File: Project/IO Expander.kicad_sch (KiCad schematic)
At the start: 32 parts, among them J801 Conn_02x08_Odd_Even, U801 MCP23017T-E_ML

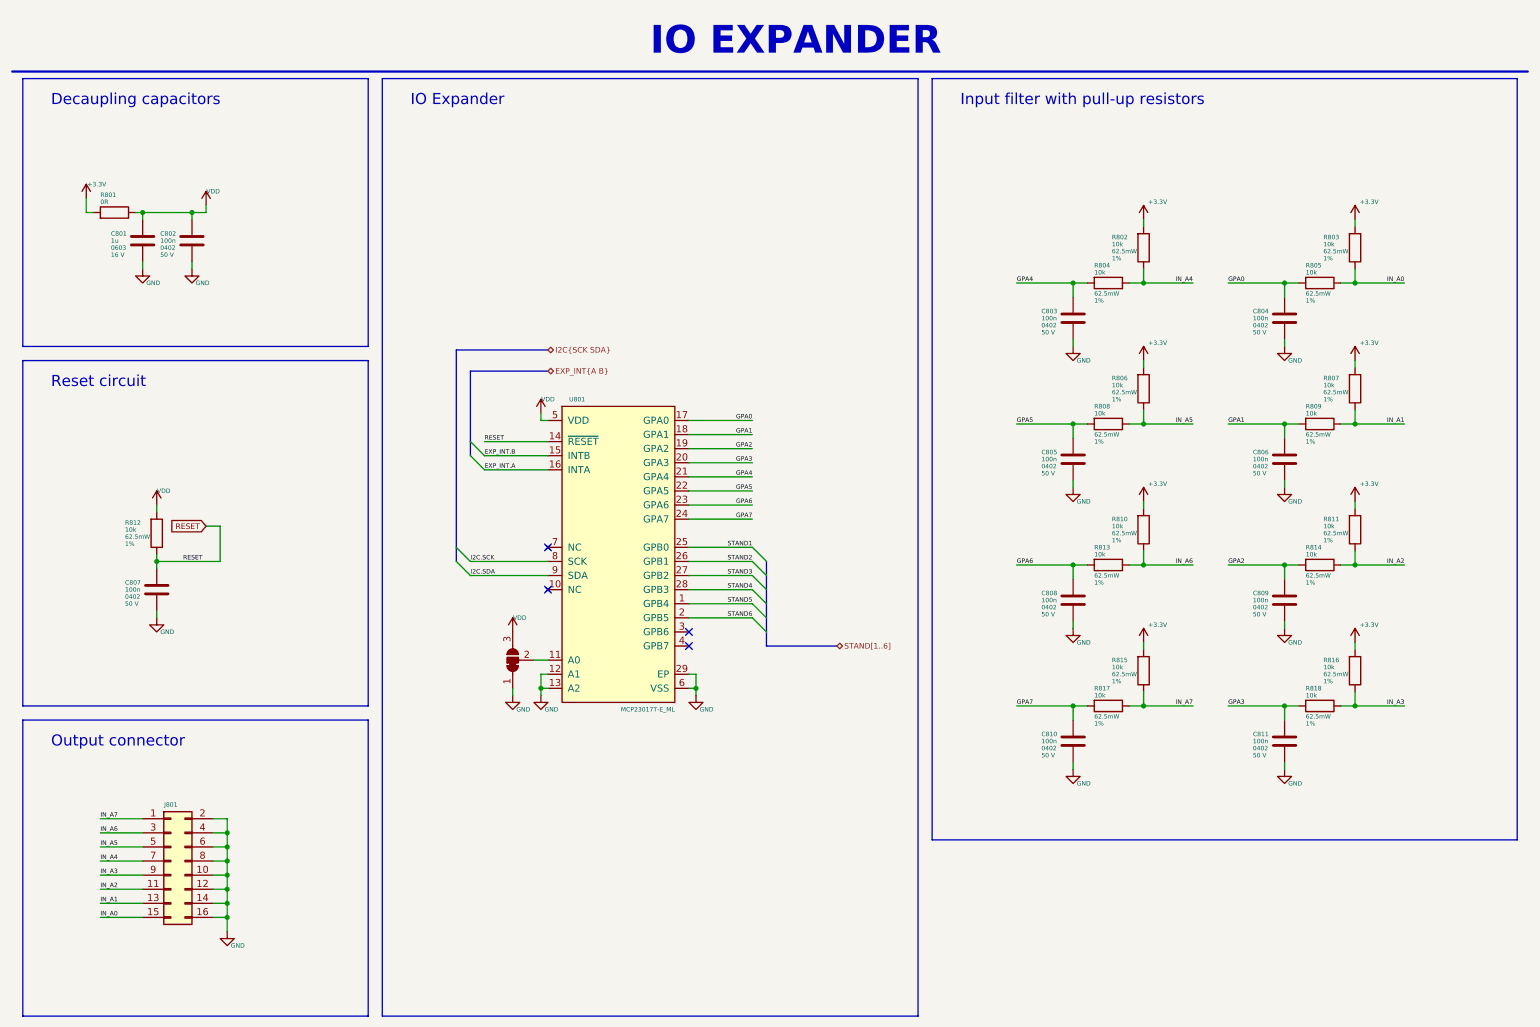
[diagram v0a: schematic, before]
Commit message: Cleaning files, added testpoints
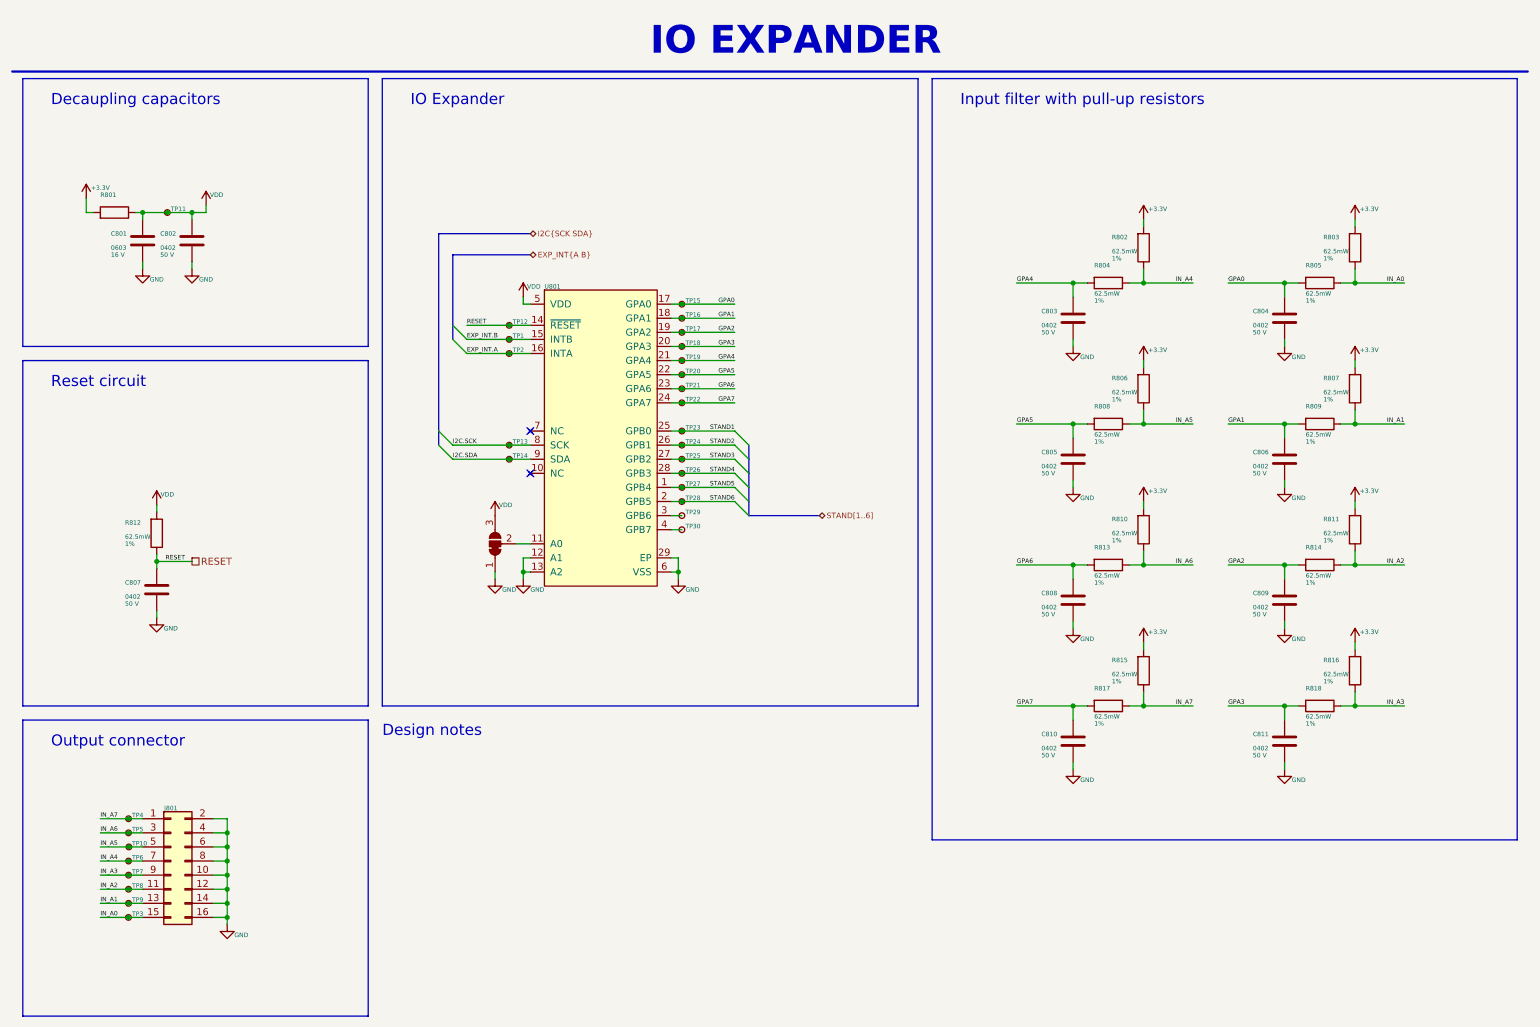
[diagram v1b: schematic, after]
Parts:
- added TP1, TP10, TP11, TP12, TP13, TP14, TP15, TP16, TP17, TP18, TP19, TP2, TP20, TP21, TP22, TP23, TP24, TP25, TP26, TP27, TP28, TP29, TP3, TP30, TP4, TP5, TP6, TP7, TP8, TP9: (no value), symbol Connector:TestPoint_Small
- C801: value 1u -> (none); footprint Capacitor_SMD:C_0603_1608Metric -> (none)
- C802, C803, C804, C805, C806, C807, C808, C809, C810, C811: value 100n -> (none); footprint Capacitor_SMD:C_0402_1005Metric -> (none)
- J801: value Conn_02x08_Odd_Even -> (none); footprint Connector_PinHeader_2.54mm:PinHeader_2x08_P2.54mm_Vertical -> (none)
- JP801: value SolderJumper_3_Bridged12 -> (none); footprint Jumper:SolderJumper-3_P1.3mm_Bridged12_RoundedPad1.0x1.5mm_NumberLabels -> (none)
- R801: value 0R -> (none); footprint Resistor_SMD:R_0402_1005Metric -> (none)
- R802, R803, R804, R805, R806, R807, R808, R809, R810, R811, R812, R813, R814, R815, R816, R817, R818: value 10k -> (none); footprint Resistor_SMD:R_0402_1005Metric -> (none)
- U801: value MCP23017T-E_ML -> (none); footprint eval_board_tmc6200-ta:MCP23017T-EML_QFN-28 -> (none)
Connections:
- net EXP_INT.A: now also TP2.1
- net EXP_INT.B: now also TP1.1
- net GPA0: now also TP15.1
- net GPA1: now also TP16.1
- net GPA2: now also TP17.1
- net GPA3: now also TP18.1
- net GPA4: now also TP19.1
- net GPA5: now also TP20.1
- net GPA6: now also TP21.1
- net GPA7: now also TP22.1
- net I2C.SCK: now also TP13.1
- net I2C.SDA: now also TP14.1
- net IN_A0: now also TP3.1
- net IN_A1: now also TP9.1
- net IN_A2: now also TP8.1
- net IN_A3: now also TP7.1
- net IN_A4: now also TP6.1
- net IN_A5: now also TP10.1
- net IN_A6: now also TP5.1
- net IN_A7: now also TP4.1
- net RESET: now also TP12.1
- net STAND1: now also TP23.1
- net STAND2: now also TP24.1
- net STAND3: now also TP25.1
- net STAND4: now also TP26.1
- net STAND5: now also TP27.1
- net STAND6: now also TP28.1
- net VDD: now also TP11.1
- net at U801.3 (GPB6): now also TP29.1
- net at U801.4 (GPB7): now also TP30.1
- no-connect marks 4 -> 2
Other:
- note added: "Design notes"
- moved on the sheet: U801
